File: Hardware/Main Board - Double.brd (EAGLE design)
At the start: 124.5 x 73.7 mm, 112 parts, among them J1 MICROMOD-2222-C, J10 MICRO-SD-PUSH-PUSH-EXT-PIN, J2 Vertical Qwiic Connector, J4 QWIIC_RIGHT_ANGLE, J5 CORTEX_JTAG_DEBUG_MINIMUM_PTH, J6 MICROMOD_FUNCTION_MAIN, J7 MICROMOD_FUNCTION_MAIN, Q1 3.1A/30V/105mΩ, U1 STG3856QTR, U2 MCP73831, U5 AP7361C-33

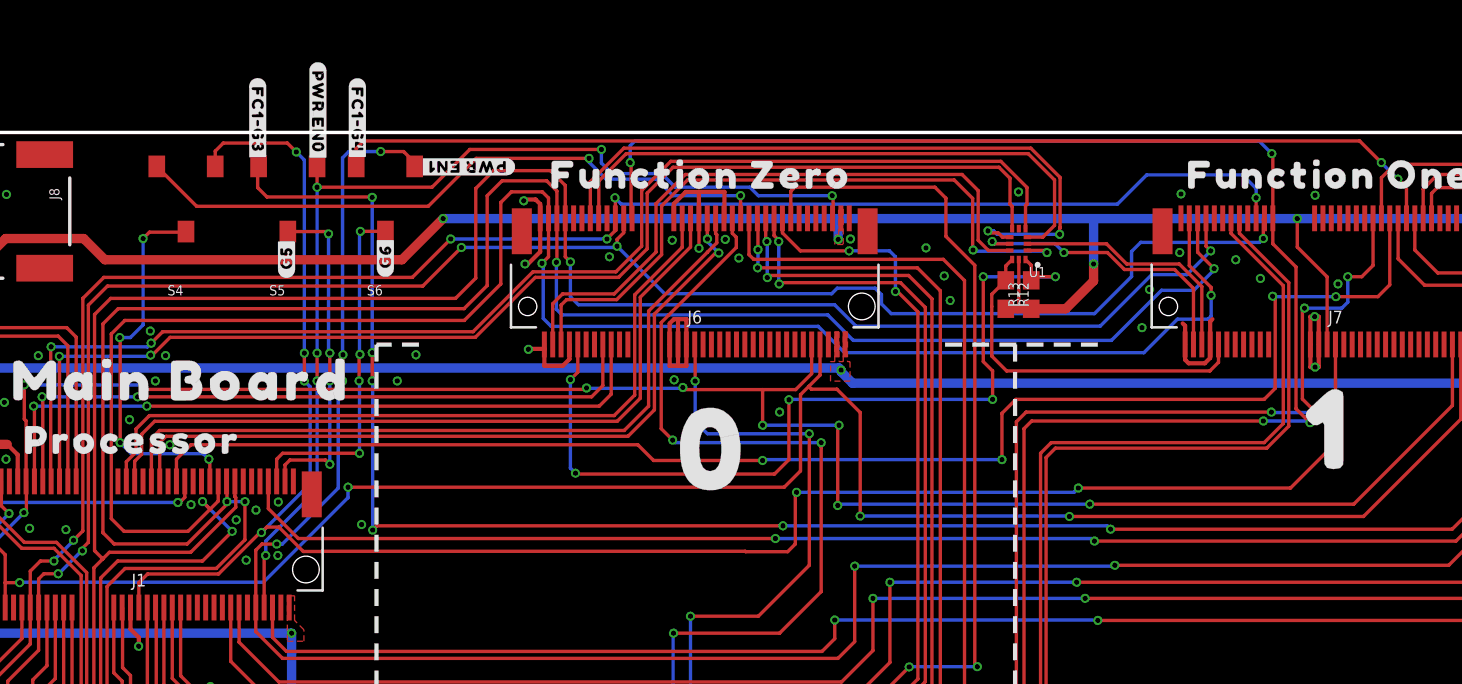
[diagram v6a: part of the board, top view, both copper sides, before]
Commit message: Flipped the switches around for better labels
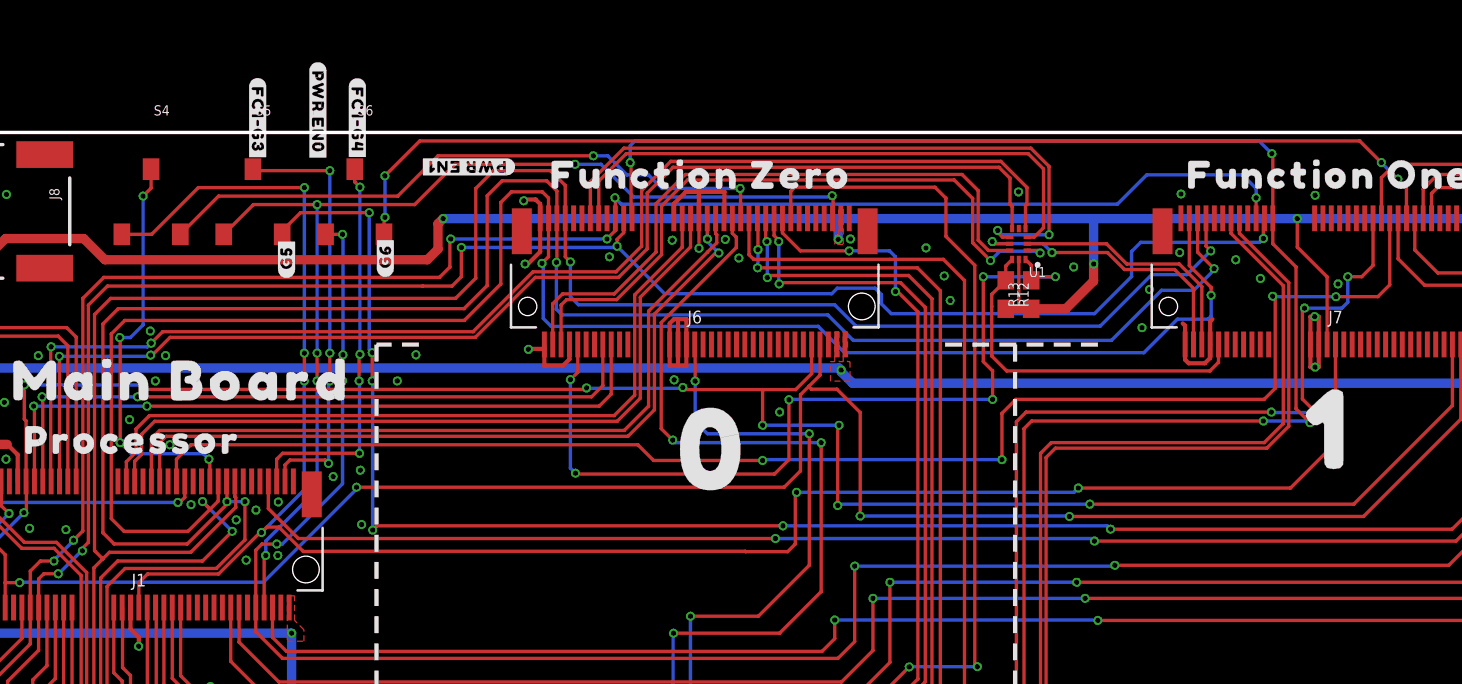
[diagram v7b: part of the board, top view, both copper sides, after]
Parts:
- moved S5 2.29 mm to (35.7, 69.6), turned to 0 degrees
- moved S4 2.29 mm to (29.6, 69.6), turned to 0 degrees
- moved S6 2.03 mm to (41.8, 69.6), turned to 0 degrees
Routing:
- net SDIO_DATA1/PWR_EN1_ALT: track 140.5 -> 132.0 mm
- net G5-JUMPER: track 20.2 -> 26.1 mm
- net G5-PROCESSOR: track 120.1 -> 116.7 mm
- net SDIO_DATA2/PWR_EN0_ALT: track 62.5 -> 65.8 mm
- net A1-PROCESSOR/!CS0!-ALT: track 116.0 -> 119.3 mm
- net G6-JUMPER: track 21.3 -> 23.6 mm
- net RX1-PROCESSOR-PLEX: track 41.1 -> 39.2 mm
- net !CS0!-PROC-JUMPER: track 23.0 -> 24.6 mm
- net !CS0!-PROCESSOR: track 39.5 -> 38.1 mm
- net G6-PROCESSOR: track 67.1 -> 68.5 mm, vias 2 -> 4
- net I2C_SCL: track 158.4 -> 159.5 mm
- net I2C_SDA: track 153.5 -> 154.5 mm
- net 3.3V: track 258.8 -> 259.7 mm
- net TX1-PROCESSOR-PLEX: track 35.5 -> 34.6 mm
- net TX1-AUX_RX-FC0-PLEX: track 41.1 -> 40.5 mm
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
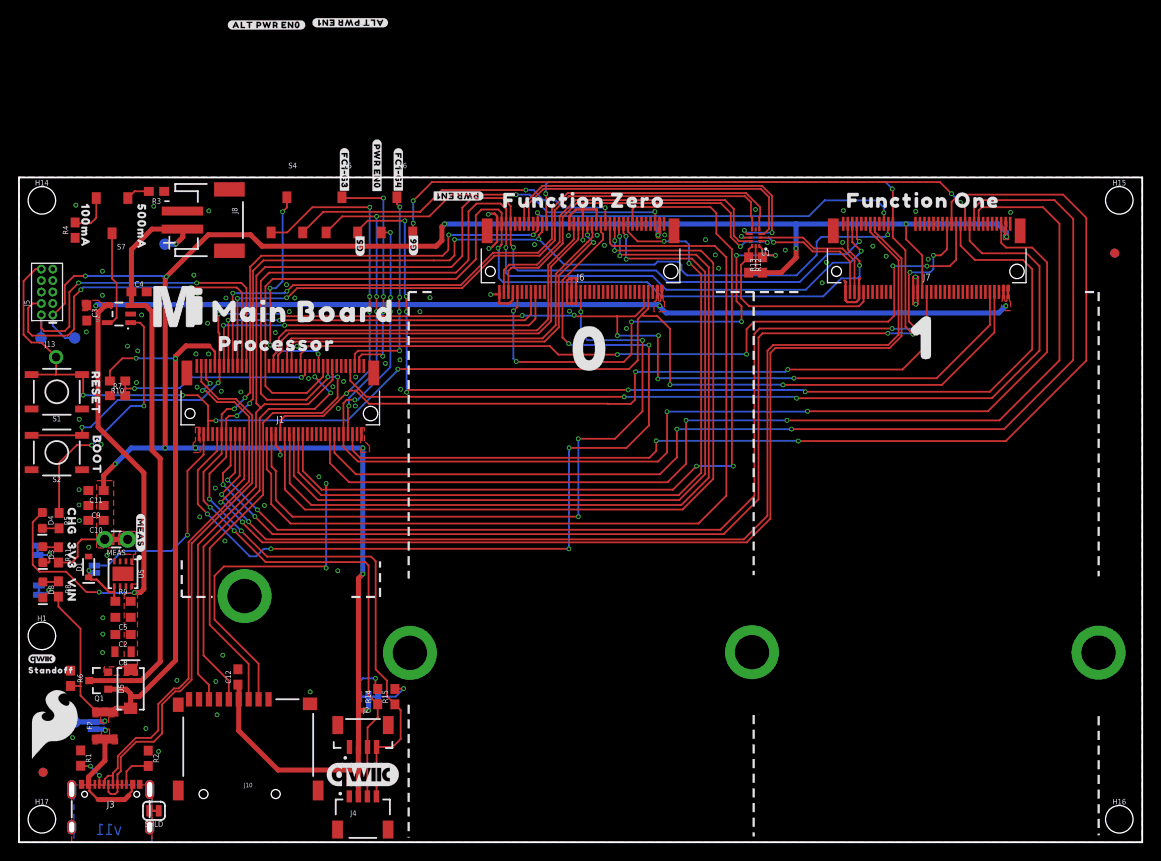
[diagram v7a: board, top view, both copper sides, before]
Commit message: Adds vias, moves traces for ground pour
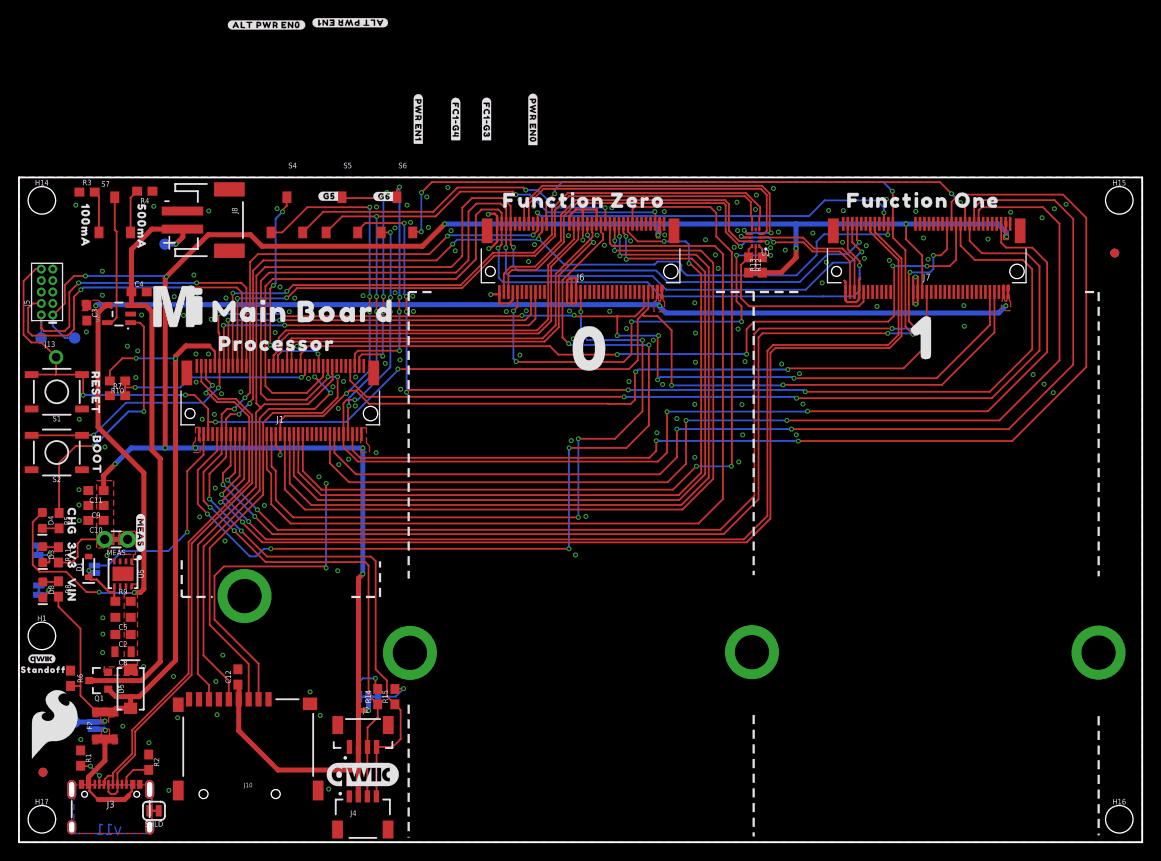
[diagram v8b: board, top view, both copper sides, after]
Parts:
- moved U$30 18.0 mm to (56.9, 80.0)
- moved U$27 16.7 mm to (51.8, 80.0)
- moved U$31 9.46 mm to (44.2, 80.0), turned to 270 degrees
- moved R4 8.85 mm to (13.9, 72.1), turned to 180 degrees
- moved U$28 8.46 mm to (48.4, 80.0)
- moved R3 7.70 mm to (7.54, 72.0), turned to 0 degrees
- moved U$32 6.39 mm to (34.4, 71.6), turned to 0 degrees
- moved U$29 6.21 mm to (40.5, 71.6), turned to 0 degrees
- moved U$23 0.84 mm to (2.72, 19.1)
- moved R2 0.43 mm to (14.4, 8.86)
- moved S7 0.27 mm to (10.5, 69.6), turned to 0 degrees
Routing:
- net N$6: track 10.8 -> 14.7 mm
- net G6-JUMPER: track 23.6 -> 25.9 mm
- net N$8: track 2.64 -> 4.67 mm
- net D-: track 59.6 -> 58.1 mm
- net D+: track 60.3 -> 58.9 mm
- net I2C_!INT!: track 164.8 -> 163.7 mm
- net !DFU-FC0!: track 51.7 -> 50.6 mm
- net I2C_SCL: track 159.5 -> 158.5 mm
- net SPI_PROCESSOR_SCK: track 155.0 -> 155.9 mm
- net 3.3V: track 259.7 -> 258.8 mm
- net I2C_SDA: track 154.5 -> 153.8 mm
- net G6-PROCESSOR: track 68.5 -> 69.0 mm
- net GND: vias 87 -> 171
